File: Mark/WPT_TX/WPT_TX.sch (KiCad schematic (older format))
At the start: 113 parts, among them J1 Conn_01x01, J10 Conn_01x01, J2 Conn_01x01, J3 Conn_Coaxial, J4 Conn_Coaxial, J5 Conn_Coaxial, J6 Conn_02x05_Odd_Even, J7 Conn_01x03, J8 Conn_01x04, J9 Conn_01x01, Q1 NMOS, Q2 NMOS, Q3 NMOS, Q4 NMOS, U1 INA240A1D, U10 LM5106, U11 MCP2515-QFN20, U12 MCP2562-E-MF, U13 LM5106, U2 LM2937IMP-3.3, U3 LM2936-5.0, U4 LM2937IMP-12, U5 LMC6032, U6 CD4043BDR, U7 BTS6142DAUMA1, U8 SN74LVC1G14DBV, U9 ATSAMD21G16B-MFT, Y1 32.7680kHz, Y2 8MHz

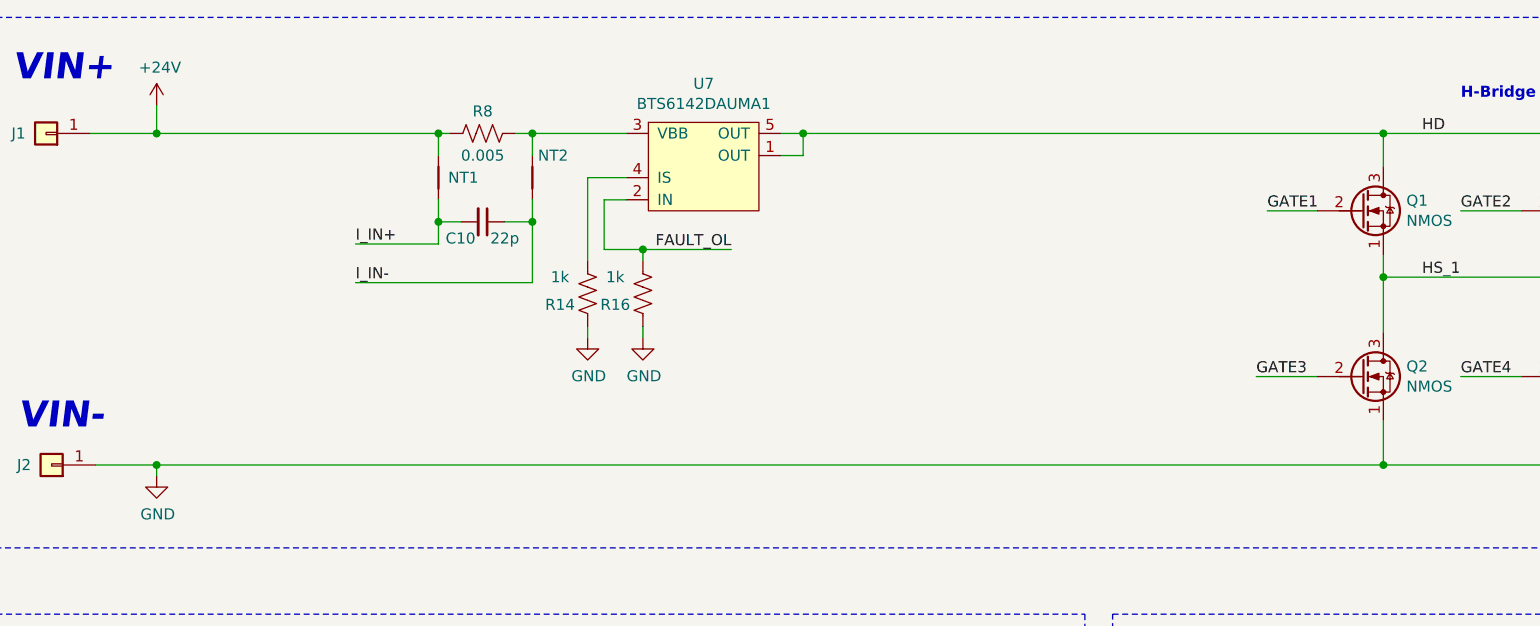
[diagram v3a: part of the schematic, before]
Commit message: Added input caps
- Forgot input capacitors, oops
- Updated sim based on cap selection, achieving 87% efficiency, low loss on caps!
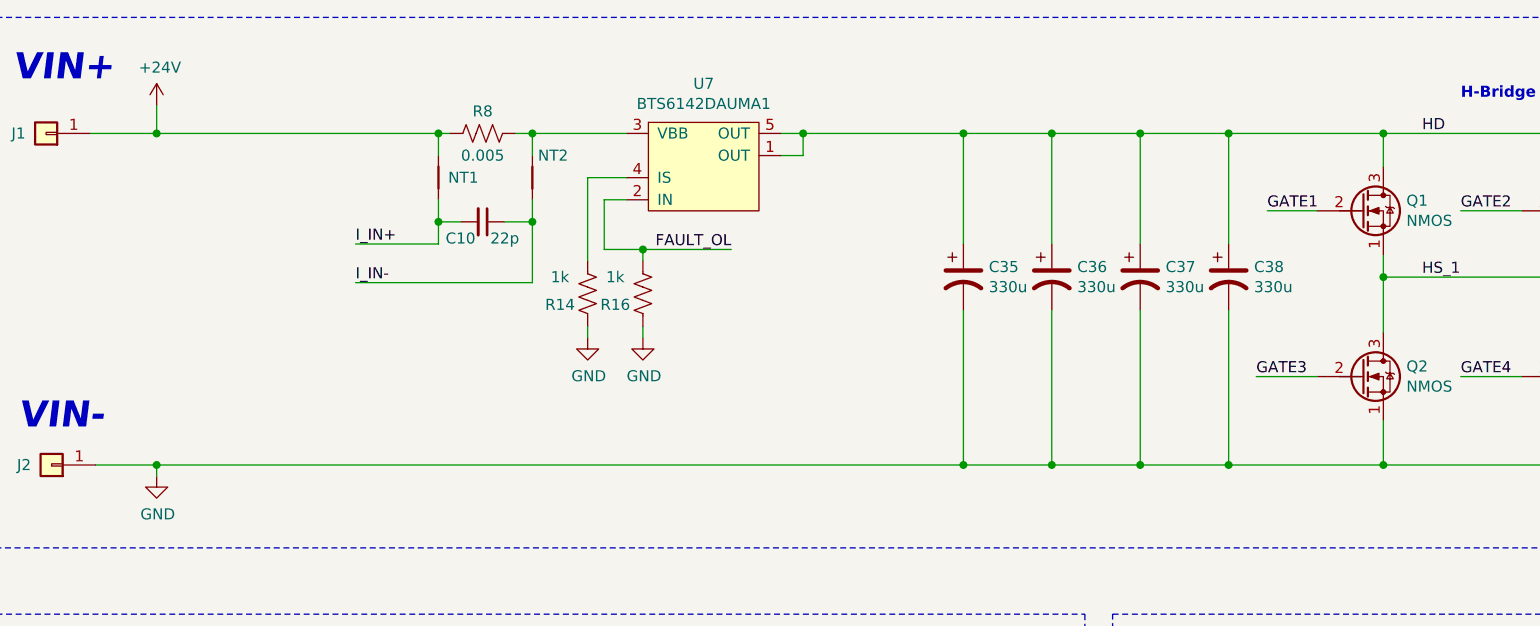
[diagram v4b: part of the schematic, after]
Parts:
- added C35, C36, C37, C38: 330u, Capacitor_SMD:CP_Elec_10x12.5, symbol Device:CP1
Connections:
- net GND: now also C35.2, C36.2, C37.2, C38.2
- net HD: now also C35.1, C36.1, C37.1, C38.1
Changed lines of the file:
@@
 Connection ~ 2100 2600
-Wire Wire Line
-	2100 2600 7650 2600
 Wire Wire Line
 	4925 1100 5025 1100
@@
 	5025 1200 5025 1100
 Connection ~ 5025 1100
-Wire Wire Line
-	5025 1100 7650 1100
 Wire Wire Line
 	8925 1100 10300 1100
@@
 Text Notes 3550 3500 0    50   ~ 10
 LED Indicators
+$Comp
+L Device:CP1 C35
+U 1 1 5FADBE10
+P 5750 1750
+F 0 "C35" H 5865 1796 50  0000 L CNN
+F 1 "330u" H 5865 1705 50  0000 L CNN
+F 2 "Capacitor_SMD:CP_Elec_10x12.5" H 5750 1750 50  0001 C CNN
+F 3 "~" H 5750 1750 50  0001 C CNN
+F 4 "493-13765-1-ND" H 5750 1750 50  0001 C CNN "Digikey"
+	1    5750 1750
+	1    0    0    -1
+$EndComp
+$Comp
+L Device:CP1 C36
+U 1 1 5FADE657
+P 6150 1750
+F 0 "C36" H 6265 1796 50  0000 L CNN
+F 1 "330u" H 6265 1705 50  0000 L CNN
+F 2 "Capacitor_SMD:CP_Elec_10x12.5" H 6150 1750 50  0001 C CNN
+F 3 "~" H 6150 1750 50  0001 C CNN
+F 4 "493-13765-1-ND" H 6150 1750 50  0001 C CNN "Digikey"
+	1    6150 1750
+	1    0    0    -1
+$EndComp
+$Comp
+L Device:CP1 C37
+U 1 1 5FADEE6A
+P 6550 1750
+F 0 "C37" H 6665 1796 50  0000 L CNN
+F 1 "330u" H 6665 1705 50  0000 L CNN
+F 2 "Capacitor_SMD:CP_Elec_10x12.5" H 6550 1750 50  0001 C CNN
+F 3 "~" H 6550 1750 50  0001 C CNN
+F 4 "493-13765-1-ND" H 6550 1750 50  0001 C CNN "Digikey"
+	1    6550 1750
+	1    0    0    -1
+$EndComp
+$Comp
+L Device:CP1 C38
+U 1 1 5FADF5ED
+P 6950 1750
+F 0 "C38" H 7065 1796 50  0000 L CNN
+F 1 "330u" H 7065 1705 50  0000 L CNN
+F 2 "Capacitor_SMD:CP_Elec_10x12.5" H 6950 1750 50  0001 C CNN
+F 3 "~" H 6950 1750 50  0001 C CNN
+F 4 "493-13765-1-ND" H 6950 1750 50  0001 C CNN "Digikey"
+	1    6950 1750
+	1    0    0    -1
+$EndComp
+Wire Wire Line
+	6950 1600 6950 1100
+Connection ~ 6950 1100
+Wire Wire Line
+	6950 1100 7650 1100
+Wire Wire Line
+	6550 1600 6550 1100
+Connection ~ 6550 1100
+Wire Wire Line
+	6550 1100 6950 1100
+Wire Wire Line
+	6150 1600 6150 1100
+Connection ~ 6150 1100
+Wire Wire Line
+	6150 1100 6550 1100
+Wire Wire Line
+	5750 1100 5750 1600
+Connection ~ 5750 1100
+Wire Wire Line
+	5750 1100 6150 1100
+Wire Wire Line
+	5750 1900 5750 2600
+Connection ~ 5750 2600
+Wire Wire Line
+	5750 2600 6150 2600
+Wire Wire Line
+	6150 1900 6150 2600
+Connection ~ 6150 2600
+Wire Wire Line
+	6150 2600 6550 2600
+Wire Wire Line
+	6550 1900 6550 2600
+Connection ~ 6550 2600
+Wire Wire Line
+	6550 2600 6950 2600
+Wire Wire Line
+	6950 1900 6950 2600
+Connection ~ 6950 2600
+Wire Wire Line
+	6950 2600 7650 2600
+Wire Wire Line
+	5025 1100 5750 1100
+Wire Wire Line
+	2100 2600 5750 2600
 $EndSCHEMATC

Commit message: Finished RX Schematic
- Finsihed RX schematic
- Completed RX BOM
- Added all footprints
- Only power resistor 3D model is outstanding, will add that later
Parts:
- TP1, TP10, TP11, TP12, TP13, TP2, TP3, TP4, TP5, TP6, TP7, TP8, TP9: footprint Testpoints:TestPoint_Loop_D1.80mm_Drill1.0mm_Beaded -> TestPoint:TestPoint_Loop_D1.80mm_Drill1.0mm_Beaded
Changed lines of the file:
@@
 F 0 "TP1" H 2908 3872 50  0000 L CNN
 F 1 "TestPoint" H 2908 3827 50  0001 L CNN
-F 2 "Testpoints:TestPoint_Loop_D1.80mm_Drill1.0mm_Beaded" H 3050 3800 50  0001 C CNN
+F 2 "TestPoint:TestPoint_Loop_D1.80mm_Drill1.0mm_Beaded" H 3050 3800 50  0001 C CNN
 F 3 "~" H 3050 3800 50  0001 C CNN
 F 4 "36-5000-ND" H 2850 3800 50  0001 C CNN "Digikey"
@@
 F 0 "TP2" H 3483 3872 50  0000 L CNN
 F 1 "TestPoint" H 3483 3827 50  0001 L CNN
-F 2 "Testpoints:TestPoint_Loop_D1.80mm_Drill1.0mm_Beaded" H 3625 3800 50  0001 C CNN
+F 2 "TestPoint:TestPoint_Loop_D1.80mm_Drill1.0mm_Beaded" H 3625 3800 50  0001 C CNN
 F 3 "~" H 3625 3800 50  0001 C CNN
 F 4 "36-5000-ND" H 3425 3800 50  0001 C CNN "Digikey"
@@
 F 0 "TP3" H 4033 3872 50  0000 L CNN
 F 1 "TestPoint" H 4033 3827 50  0001 L CNN
-F 2 "Testpoints:TestPoint_Loop_D1.80mm_Drill1.0mm_Beaded" H 4175 3800 50  0001 C CNN
+F 2 "TestPoint:TestPoint_Loop_D1.80mm_Drill1.0mm_Beaded" H 4175 3800 50  0001 C CNN
 F 3 "~" H 4175 3800 50  0001 C CNN
 F 4 "36-5000-ND" H 3975 3800 50  0001 C CNN "Digikey"
@@
 F 0 "TP4" H 4533 3872 50  0000 L CNN
 F 1 "TestPoint" H 4533 3827 50  0001 L CNN
-F 2 "Testpoints:TestPoint_Loop_D1.80mm_Drill1.0mm_Beaded" H 4675 3800 50  0001 C CNN
+F 2 "TestPoint:TestPoint_Loop_D1.80mm_Drill1.0mm_Beaded" H 4675 3800 50  0001 C CNN
 F 3 "~" H 4675 3800 50  0001 C CNN
 F 4 "36-5000-ND" H 4475 3800 50  0001 C CNN "Digikey"
@@
 F 0 "TP5" H 4608 4747 50  0000 L CNN
 F 1 "TestPoint" H 4608 4702 50  0001 L CNN
-F 2 "Testpoints:TestPoint_Loop_D1.80mm_Drill1.0mm_Beaded" H 4750 4675 50  0001 C CNN
+F 2 "TestPoint:TestPoint_Loop_D1.80mm_Drill1.0mm_Beaded" H 4750 4675 50  0001 C CNN
 F 3 "~" H 4750 4675 50  0001 C CNN
 F 4 "36-5001-ND" H 4550 4675 50  0001 C CNN "Digikey"
@@
 F 0 "TP7" H 5408 4772 50  0000 L CNN
 F 1 "TestPoint" H 5408 4727 50  0001 L CNN
-F 2 "Testpoints:TestPoint_Loop_D1.80mm_Drill1.0mm_Beaded" H 5550 4700 50  0001 C CNN
+F 2 "TestPoint:TestPoint_Loop_D1.80mm_Drill1.0mm_Beaded" H 5550 4700 50  0001 C CNN
 F 3 "~" H 5550 4700 50  0001 C CNN
 F 4 "36-5001-ND" H 5350 4700 50  0001 C CNN "Digikey"
@@
 F 0 "TP6" H 5108 3897 50  0000 L CNN
 F 1 "TestPoint" H 5108 3852 50  0001 L CNN
-F 2 "Testpoints:TestPoint_Loop_D1.80mm_Drill1.0mm_Beaded" H 5250 3825 50  0001 C CNN
+F 2 "TestPoint:TestPoint_Loop_D1.80mm_Drill1.0mm_Beaded" H 5250 3825 50  0001 C CNN
 F 3 "~" H 5250 3825 50  0001 C CNN
 F 4 "36-5001-ND" H 5050 3825 50  0001 C CNN "Digikey"
@@
 F 0 "TP12" H 10358 1072 50  0000 L CNN
 F 1 "TestPoint" H 10358 1027 50  0001 L CNN
-F 2 "Testpoints:TestPoint_Loop_D1.80mm_Drill1.0mm_Beaded" H 10500 1000 50  0001 C CNN
+F 2 "TestPoint:TestPoint_Loop_D1.80mm_Drill1.0mm_Beaded" H 10500 1000 50  0001 C CNN
 F 3 "~" H 10500 1000 50  0001 C CNN
 F 4 "36-5117-ND" H 10300 1000 50  0001 C CNN "Digikey"
@@
 F 0 "TP13" H 10358 2747 50  0000 L CNN
 F 1 "TestPoint" H 10358 2702 50  0001 L CNN
-F 2 "Testpoints:TestPoint_Loop_D1.80mm_Drill1.0mm_Beaded" H 10500 2675 50  0001 C CNN
+F 2 "TestPoint:TestPoint_Loop_D1.80mm_Drill1.0mm_Beaded" H 10500 2675 50  0001 C CNN
 F 3 "~" H 10500 2675 50  0001 C CNN
 F 4 "36-5117-ND" H 10300 2675 50  0001 C CNN "Digikey"
@@
 F 0 "TP8" H 6658 9272 50  0000 L CNN
 F 1 "TestPoint" H 6658 9227 50  0001 L CNN
-F 2 "Testpoints:TestPoint_Loop_D1.80mm_Drill1.0mm_Beaded" H 6800 9200 50  0001 C CNN
+F 2 "TestPoint:TestPoint_Loop_D1.80mm_Drill1.0mm_Beaded" H 6800 9200 50  0001 C CNN
 F 3 "~" H 6800 9200 50  0001 C CNN
 F 4 "36-5117-ND" H 6600 9200 50  0001 C CNN "Digikey"
@@
 F 0 "TP9" H 6542 9497 50  0000 R CNN
 F 1 "TestPoint" H 6658 9452 50  0001 L CNN
-F 2 "Testpoints:TestPoint_Loop_D1.80mm_Drill1.0mm_Beaded" H 6800 9425 50  0001 C CNN
+F 2 "TestPoint:TestPoint_Loop_D1.80mm_Drill1.0mm_Beaded" H 6800 9425 50  0001 C CNN
 F 3 "~" H 6800 9425 50  0001 C CNN
 F 4 "36-5117-ND" H 6600 9425 50  0001 C CNN "Digikey"
@@
 F 0 "TP10" H 6933 8422 50  0000 L CNN
 F 1 "TestPoint" H 6933 8377 50  0001 L CNN
-F 2 "Testpoints:TestPoint_Loop_D1.80mm_Drill1.0mm_Beaded" H 7075 8350 50  0001 C CNN
+F 2 "TestPoint:TestPoint_Loop_D1.80mm_Drill1.0mm_Beaded" H 7075 8350 50  0001 C CNN
 F 3 "~" H 7075 8350 50  0001 C CNN
 F 4 "36-5117-ND" H 6875 8350 50  0001 C CNN "Digikey"
@@
 F 0 "TP11" H 9458 8722 50  0000 L CNN
 F 1 "TestPoint" H 9458 8677 50  0001 L CNN
-F 2 "Testpoints:TestPoint_Loop_D1.80mm_Drill1.0mm_Beaded" H 9600 8650 50  0001 C CNN
+F 2 "TestPoint:TestPoint_Loop_D1.80mm_Drill1.0mm_Beaded" H 9600 8650 50  0001 C CNN
 F 3 "~" H 9600 8650 50  0001 C CNN
 F 4 "36-5117-ND" H 9400 8650 50  0001 C CNN "Digikey"

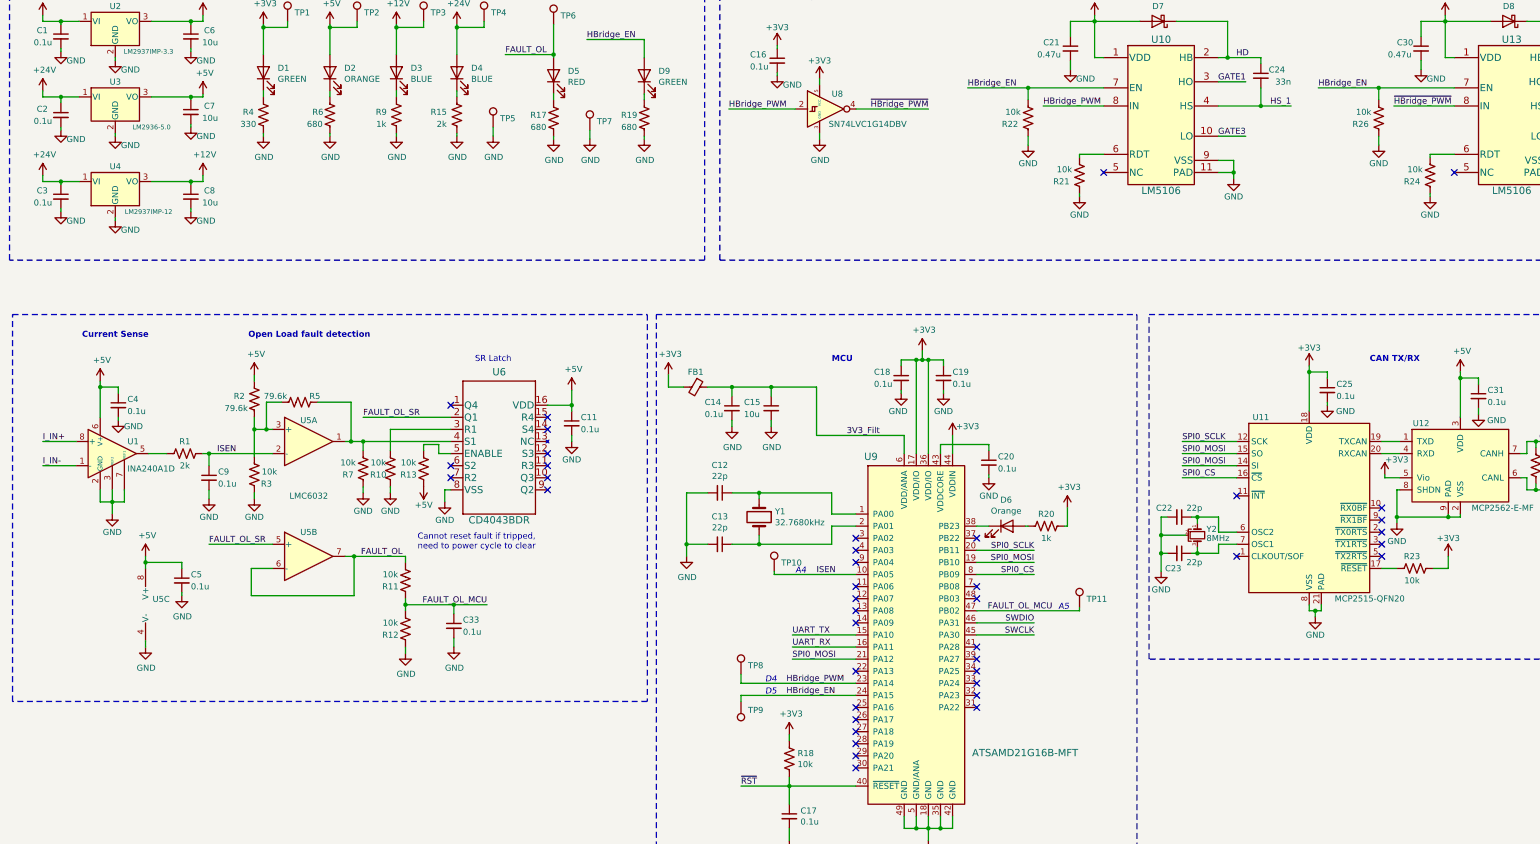
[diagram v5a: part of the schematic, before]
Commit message: Layout
- Finished expected layout. Going for routing next.
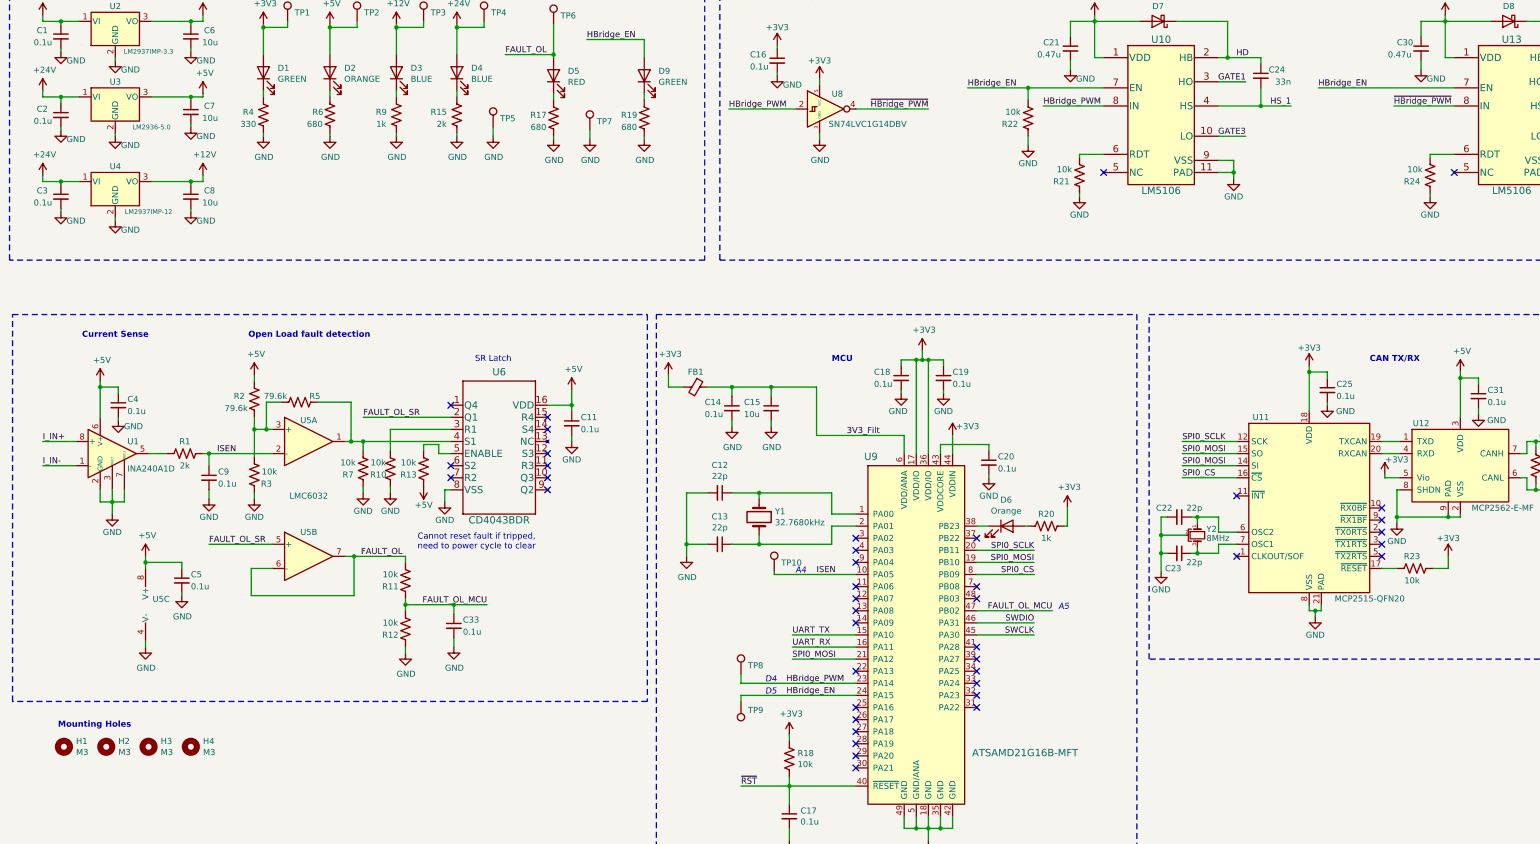
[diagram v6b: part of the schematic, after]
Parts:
- removed R26: 10k, Resistor_SMD:R_0603_1608Metric, symbol WPT_TX-rescue:R_US-Device
- removed TP11: TestPoint, TestPoint:TestPoint_Loop_D1.80mm_Drill1.0mm_Beaded, symbol WPT_TX-rescue:TestPoint-Connector
- added H1, H2, H3, H4: M3, MountingHole:MountingHole_3.2mm_M3_DIN965_Pad, symbol Mechanical:MountingHole
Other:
- note added: "Mounting Holes"
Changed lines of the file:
@@
 Text Label 11375 4350 0    50   ~ 0
 HBridge_EN
-Wire Wire Line
-	11375 4350 11875 4350
 NoConn ~ 12500 5050
 Wire Wire Line
@@
 Text Label 12000 4500 0    50   ~ 0
 ~HBridge_PWM~
-Wire Wire Line
-	11875 4350 11875 4450
-Connection ~ 11875 4350
-Wire Wire Line
-	11875 4350 12500 4350
-Wire Wire Line
-	11875 4750 11875 4825
-$Comp
-L WPT_TX-rescue:GND-power #PWR075
-U 1 1 61DE8533
-P 11875 4825
-F 0 "#PWR075" H 11875 4575 50  0001 C CNN
-F 1 "GND" H 11875 4675 50  0000 C CNN
-F 2 "" H 11875 4825 50  0001 C CNN
-F 3 "" H 11875 4825 50  0001 C CNN
-	1    11875 4825
-	1    0    0    -1
-$EndComp
 $Comp
 L WPT_TX-rescue:+12V-power #PWR080
@@
 	6600 9275 6600 9200
 Wire Wire Line
-	9400 8650 9400 8675
-Wire Wire Line
-	8550 8675 9400 8675
+	8550 8675 9175 8675
 Wire Wire Line
 	6875 8350 6875 8375
@@
 F 4 "36-5117-ND" H 6875 8350 50  0001 C CNN "Digikey"
 	1    6875 8350
-	1    0    0    -1
-$EndComp
-$Comp
-L WPT_TX-rescue:TestPoint-Connector TP11
-U 1 1 6286C102
-P 9400 8650
-F 0 "TP11" H 9458 8722 50  0000 L CNN
-F 1 "TestPoint" H 9458 8677 50  0001 L CNN
-F 2 "TestPoint:TestPoint_Loop_D1.80mm_Drill1.0mm_Beaded" H 9600 8650 50  0001 C CNN
-F 3 "~" H 9600 8650 50  0001 C CNN
-F 4 "36-5117-ND" H 9400 8650 50  0001 C CNN "Digikey"
-	1    9400 8650
 	1    0    0    -1
 $EndComp
@@
 $EndComp
 $Comp
-L WPT_TX-rescue:R_US-Device R26
-U 1 1 5FCE5107
-P 11875 4600
-F 0 "R26" H 12025 4650 50  0000 C CNN
-F 1 "10k" H 12000 4550 50  0000 C CNN
-F 2 "Resistor_SMD:R_0603_1608Metric" V 11915 4590 50  0001 C CNN
-F 3 "~" H 11875 4600 50  0001 C CNN
-F 4 "RHM10KDCT-ND" H 11875 4600 50  0001 C CNN "Digikey"
-	1    11875 4600
-	-1   0    0    1
-$EndComp
-$Comp
 L WPT_TX-rescue:C_Small-Device C33
 U 1 1 5FCF14F7
@@
 Wire Wire Line
 	2100 2600 5750 2600
+$Comp
+L Mechanical:MountingHole H1
+U 1 1 5FE274E2
+P 1000 9800
+F 0 "H1" H 1100 9846 50  0000 L CNN
+F 1 "M3" H 1100 9755 50  0000 L CNN
+F 2 "MountingHole:MountingHole_3.2mm_M3_DIN965_Pad" H 1000 9800 50  0001 C CNN
+F 3 "~" H 1000 9800 50  0001 C CNN
+	1    1000 9800
+	1    0    0    -1
+$EndComp
+$Comp
+L Mechanical:MountingHole H2
+U 1 1 5FE27746
+P 1350 9800
+F 0 "H2" H 1450 9846 50  0000 L CNN
+F 1 "M3" H 1450 9755 50  0000 L CNN
+F 2 "MountingHole:MountingHole_3.2mm_M3_DIN965_Pad" H 1350 9800 50  0001 C CNN
+F 3 "~" H 1350 9800 50  0001 C CNN
+	1    1350 9800
+	1    0    0    -1
+$EndComp
+$Comp
+L Mechanical:MountingHole H3
+U 1 1 5FE2784E
+P 1700 9800
+F 0 "H3" H 1800 9846 50  0000 L CNN
+F 1 "M3" H 1800 9755 50  0000 L CNN
+F 2 "MountingHole:MountingHole_3.2mm_M3_DIN965_Pad" H 1700 9800 50  0001 C CNN
+F 3 "~" H 1700 9800 50  0001 C CNN
+	1    1700 9800
+	1    0    0    -1
+$EndComp
+$Comp
+L Mechanical:MountingHole H4
+U 1 1 5FE279EC
+P 2050 9800
+F 0 "H4" H 2150 9846 50  0000 L CNN
+F 1 "M3" H 2150 9755 50  0000 L CNN
+F 2 "MountingHole:MountingHole_3.2mm_M3_DIN965_Pad" H 2050 9800 50  0001 C CNN
+F 3 "~" H 2050 9800 50  0001 C CNN
+	1    2050 9800
+	1    0    0    -1
+$EndComp
+Text Notes 950  9650 0    50   ~ 10
+Mounting Holes
+Wire Wire Line
+	11375 4350 12500 4350
 $EndSCHEMATC
